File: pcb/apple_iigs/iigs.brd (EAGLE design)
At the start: 46 x 52 mm, 15 parts, among them J1 ATX24RH

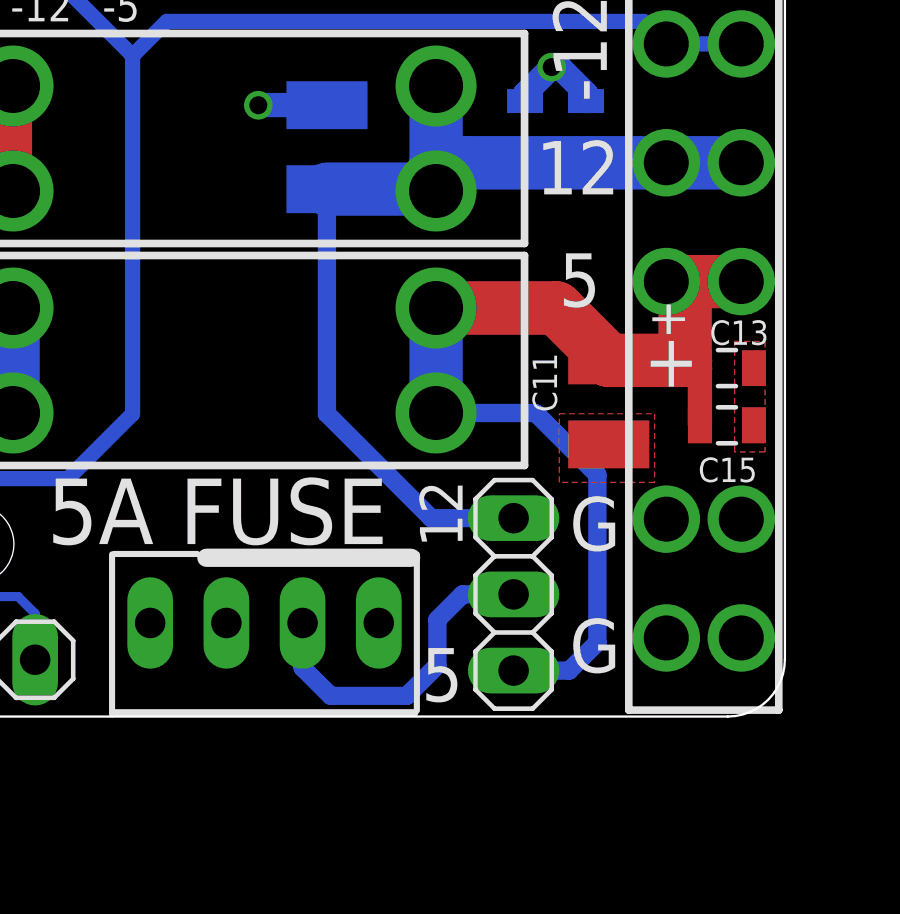
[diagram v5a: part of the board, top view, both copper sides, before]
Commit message: removed fan voltage selector
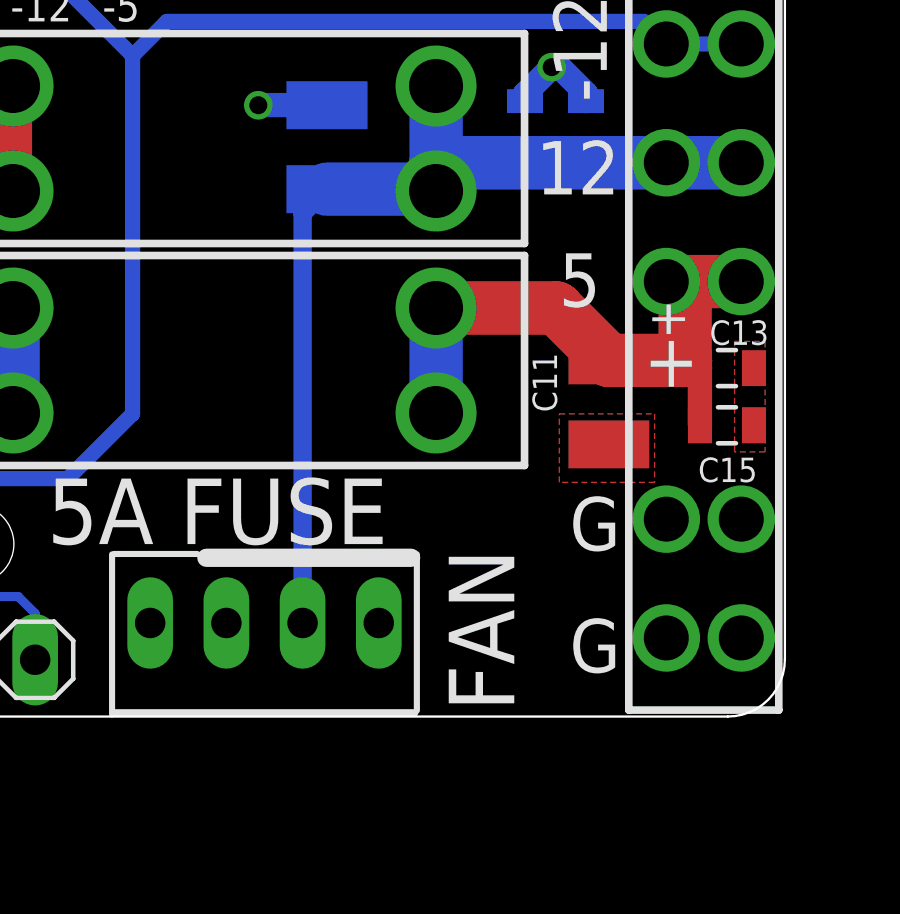
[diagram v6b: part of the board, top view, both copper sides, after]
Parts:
- removed JP2: (no value), pinhead:1X03
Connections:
- removed net N$1: JP2.2, JP4.2
- net +12V: now also JP4.2; no longer JP2.3
- net +5V: no longer JP2.1
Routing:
- net +5V: track 38.5 -> 23.5 mm
- net N$1: track 11.2 -> 0.00 mm
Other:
- board text added: "FAN"
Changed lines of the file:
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@@
 <text x="33.919" y="39.862" size="2.1844" layer="25" distance="35" align="center">+</text>
 <text x="30.862" y="39.597" size="1.4224" layer="25" distance="35" align="center">1uF</text>
-<text x="34.5462" y="18.256" size="1.4224" layer="25" distance="35" rot="R270" align="center">12</text>
-<text x="34.576" y="12.8932" size="1.778" layer="25" distance="35" align="center">5</text>
 <text x="18.923" y="35.179" size="1.016" layer="25" distance="35" align="center">G</text>
 <text x="21.209" y="35.179" size="1.016" layer="25" distance="35" align="center">-12</text>
@@
 <hole x="37.25" y="38" drill="2.6"/>
 <text x="42.212" y="23.3852" size="1.778" layer="25" distance="35" align="center">+</text>
+<text x="35.888" y="14.383" size="2.1844" layer="25" distance="35" rot="R270" align="center">FAN</text>
 </plain>
 <attributes>
@@
 <element name="U$7" library="atx4vc" package="3.96_FEMALE_IIGS_GAP" value="3.96_FEM_IIGS" x="43.297" y="26" smashed="yes" rot="R270"/>
 <element name="JP4" library="appleii" package="1X04" value="" x="28.653" y="14.619" smashed="yes" rot="R180"/>
-<element name="JP2" library="pinhead" library_urn="urn:adsk.eagle:library:325" package="1X03" package3d_urn="urn:adsk.eagle:package:22458/2" value="" x="36.957" y="15.572" smashed="yes" rot="R90">
-<attribute name="POPULARITY" value="92" x="36.957" y="15.572" size="1.778" layer="27" rot="R90" display="off"/>
-<attribute name="VALUE" x="40.132" y="11.762" size="1.27" layer="27" rot="R90"/>
-</element>
 <element name="C11" library="clock" package="C1210" value="47uF" x="40.132" y="21.971" smashed="yes" rot="R270">
 <attribute name="NAME" x="37.592" y="23.622" size="0.8128" layer="25" rot="R270"/>
@@
 <contactref element="U$7" pad="41"/>
 <contactref element="U$7" pad="40"/>
-<contactref element="JP2" pad="1"/>
 <wire x1="34.372" y1="25.118" x2="34.372" y2="21.618" width="1.778" layer="16"/>
-<wire x1="34.372" y1="21.618" x2="37.691" y2="21.618" width="0.6096" layer="16"/>
-<wire x1="37.691" y1="21.618" x2="39.751" y2="19.558" width="0.6096" layer="16"/>
-<wire x1="39.751" y1="19.558" x2="39.751" y2="13.97" width="0.6096" layer="16"/>
-<wire x1="38.813" y1="13.032" x2="36.957" y2="13.032" width="0.6096" layer="16"/>
-<wire x1="39.751" y1="13.97" x2="38.813" y2="13.032" width="0.6096" layer="16"/>
 <contactref element="C11" pad="1"/>
 <contactref element="C13" pad="2"/>
@@
 <contactref element="U$7" pad="51"/>
 <contactref element="U$7" pad="50"/>
-<contactref element="JP2" pad="3"/>
 <wire x1="34.372" y1="32.518" x2="34.372" y2="29.018" width="1.778" layer="16"/>
 <wire x1="34.372" y1="29.018" x2="34.372" y2="29.96" width="1.778" layer="16"/>
 <wire x1="42.047" y1="29.96" x2="44.547" y2="29.96" width="1.778" layer="16"/>
 <wire x1="34.372" y1="29.018" x2="33.717" y2="29.018" width="0.6096" layer="16"/>
-<wire x1="34.212" y1="18.112" x2="36.957" y2="18.112" width="0.6096" layer="16"/>
-<wire x1="30.734" y1="21.59" x2="34.212" y2="18.112" width="0.6096" layer="16"/>
 <contactref element="C1" pad="1"/>
 <contactref element="C2" pad="2"/>
@@
 <wire x1="34.372" y1="29.018" x2="35.314" y2="29.96" width="1.778" layer="16"/>
 <wire x1="35.314" y1="29.96" x2="42.047" y2="29.96" width="1.778" layer="16"/>
-<wire x1="30.734" y1="21.59" x2="30.734" y2="29.08" width="0.6096" layer="16"/>
+<wire x1="30.734" y1="29.08" x2="29.923" y2="28.269" width="0.6096" layer="16"/>
+<wire x1="29.923" y1="28.269" x2="29.923" y2="14.619" width="0.6096" layer="16"/>
 <wire x1="39.37" y1="30.215" x2="37.338" y2="30.215" width="0.6096" layer="16"/>
 <wire x1="39.37" y1="30.215" x2="41.792" y2="30.215" width="0.6096" layer="16"/>
 <wire x1="41.792" y1="30.215" x2="42.047" y2="29.96" width="0.6096" layer="16"/>
+<contactref element="JP4" pad="2"/>
 </signal>
 <signal name="N$5">
@@
 <wire x1="24.76499375" y1="37.465" x2="28.558" y2="37.465" width="0.508" layer="16"/>
 </signal>
-<signal name="N$1">
-<contactref element="JP4" pad="2"/>
-<contactref element="JP2" pad="2"/>
-<wire x1="36.957" y1="15.572" x2="35.257" y2="15.572" width="0.6096" layer="16"/>
-<wire x1="35.257" y1="15.572" x2="34.417" y2="14.732" width="0.6096" layer="16"/>
-<wire x1="34.417" y1="14.732" x2="34.417" y2="13.208" width="0.6096" layer="16"/>
-<wire x1="33.401" y1="12.192" x2="30.861" y2="12.192" width="0.6096" layer="16"/>
-<wire x1="30.861" y1="12.192" x2="29.923" y2="13.13" width="0.6096" layer="16"/>
-<wire x1="29.923" y1="13.13" x2="29.923" y2="14.619" width="0.6096" layer="16"/>
-<wire x1="34.417" y1="13.208" x2="33.401" y2="12.192" width="0.6096" layer="16"/>
-</signal>
 </signals>
